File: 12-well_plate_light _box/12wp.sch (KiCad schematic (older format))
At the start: 7 parts

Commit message: added single well
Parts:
- U?: symbol SAM32:SAM32 -> 12wp-rescue:SAM32-SAM32
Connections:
- net labels added: OE
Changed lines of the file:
@@
 EESchema Schematic File Version 4
 LIBS:12wp-cache
-EELAYER 29 0
+EELAYER 30 0
 EELAYER END
 $Descr USLedger 17000 11000
@@
 	7700 7200 7900 7200
 $Comp
-L SAM32:SAM32 U?
+L 12wp-rescue:SAM32-SAM32 U?
 U 1 1 5E784C62
 P 7150 2200
@@
 Wire Wire Line
 	8350 6500 9400 6500
+Text Label 6350 2650 2    50   ~ 0
+OE
+Text Label 6900 7100 2    50   ~ 0
+OE
 $EndSCHEMATC

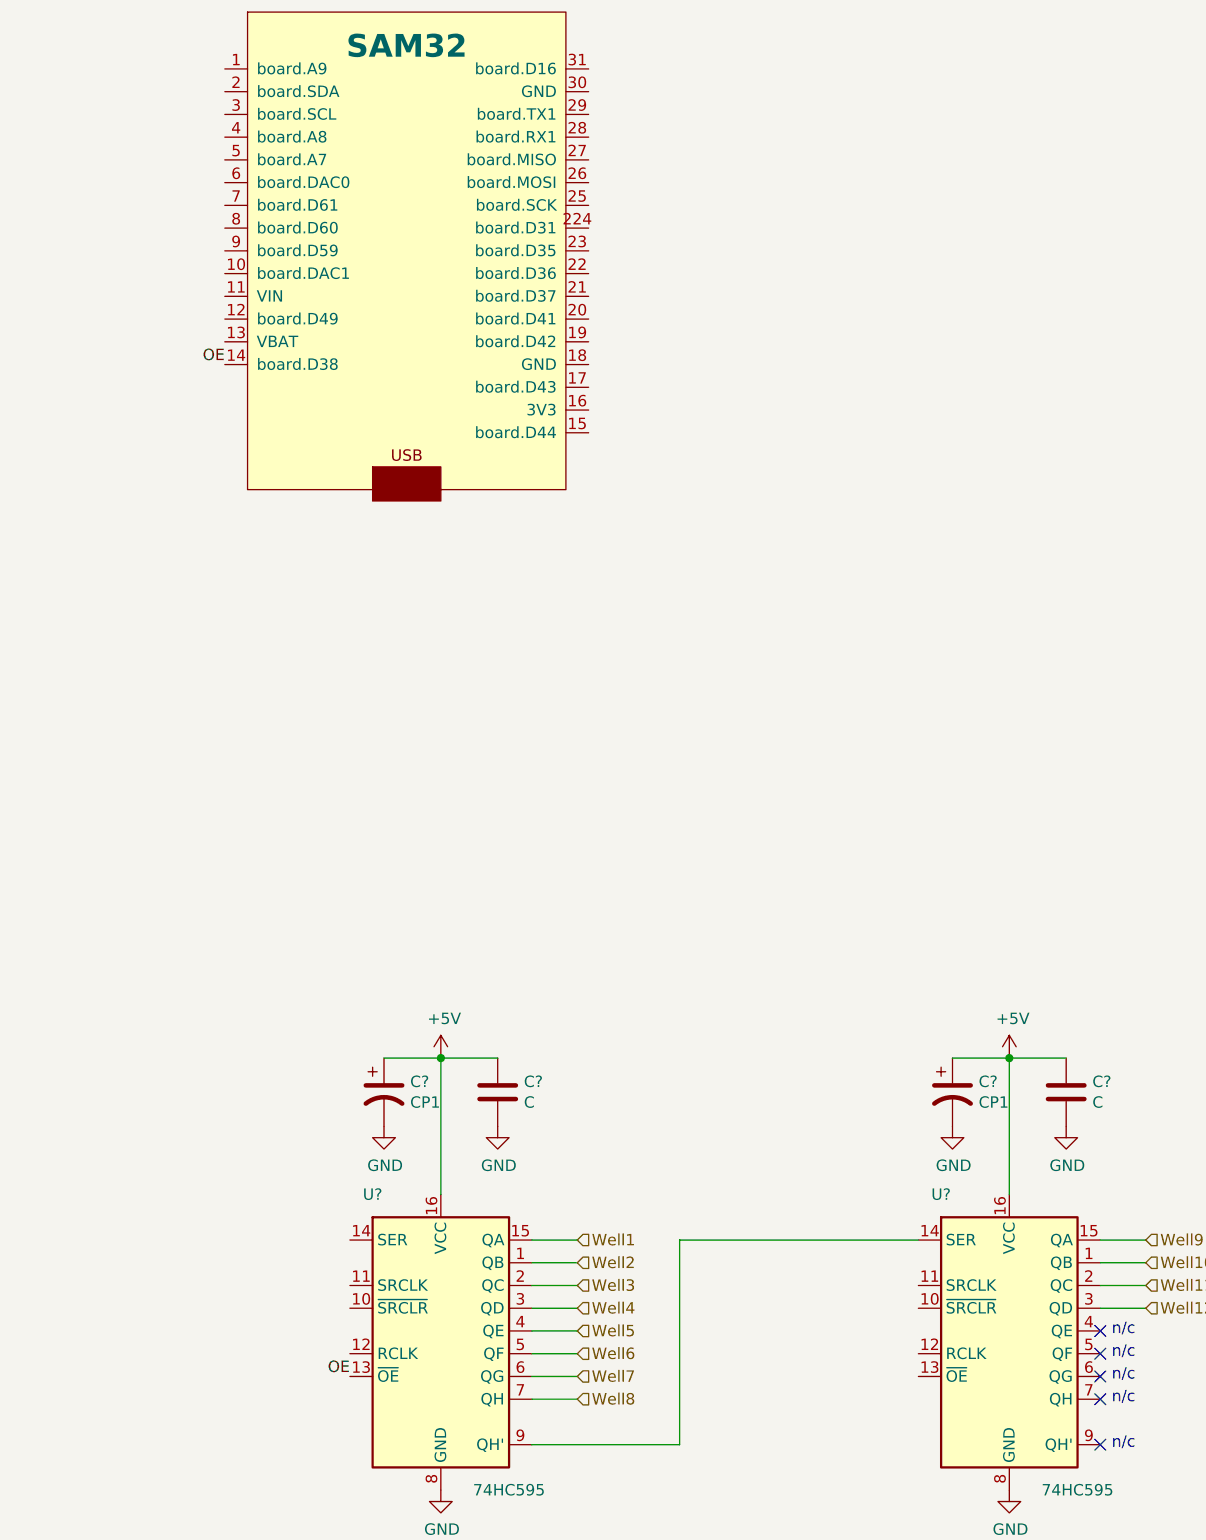
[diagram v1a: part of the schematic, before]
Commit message: added shift register controls
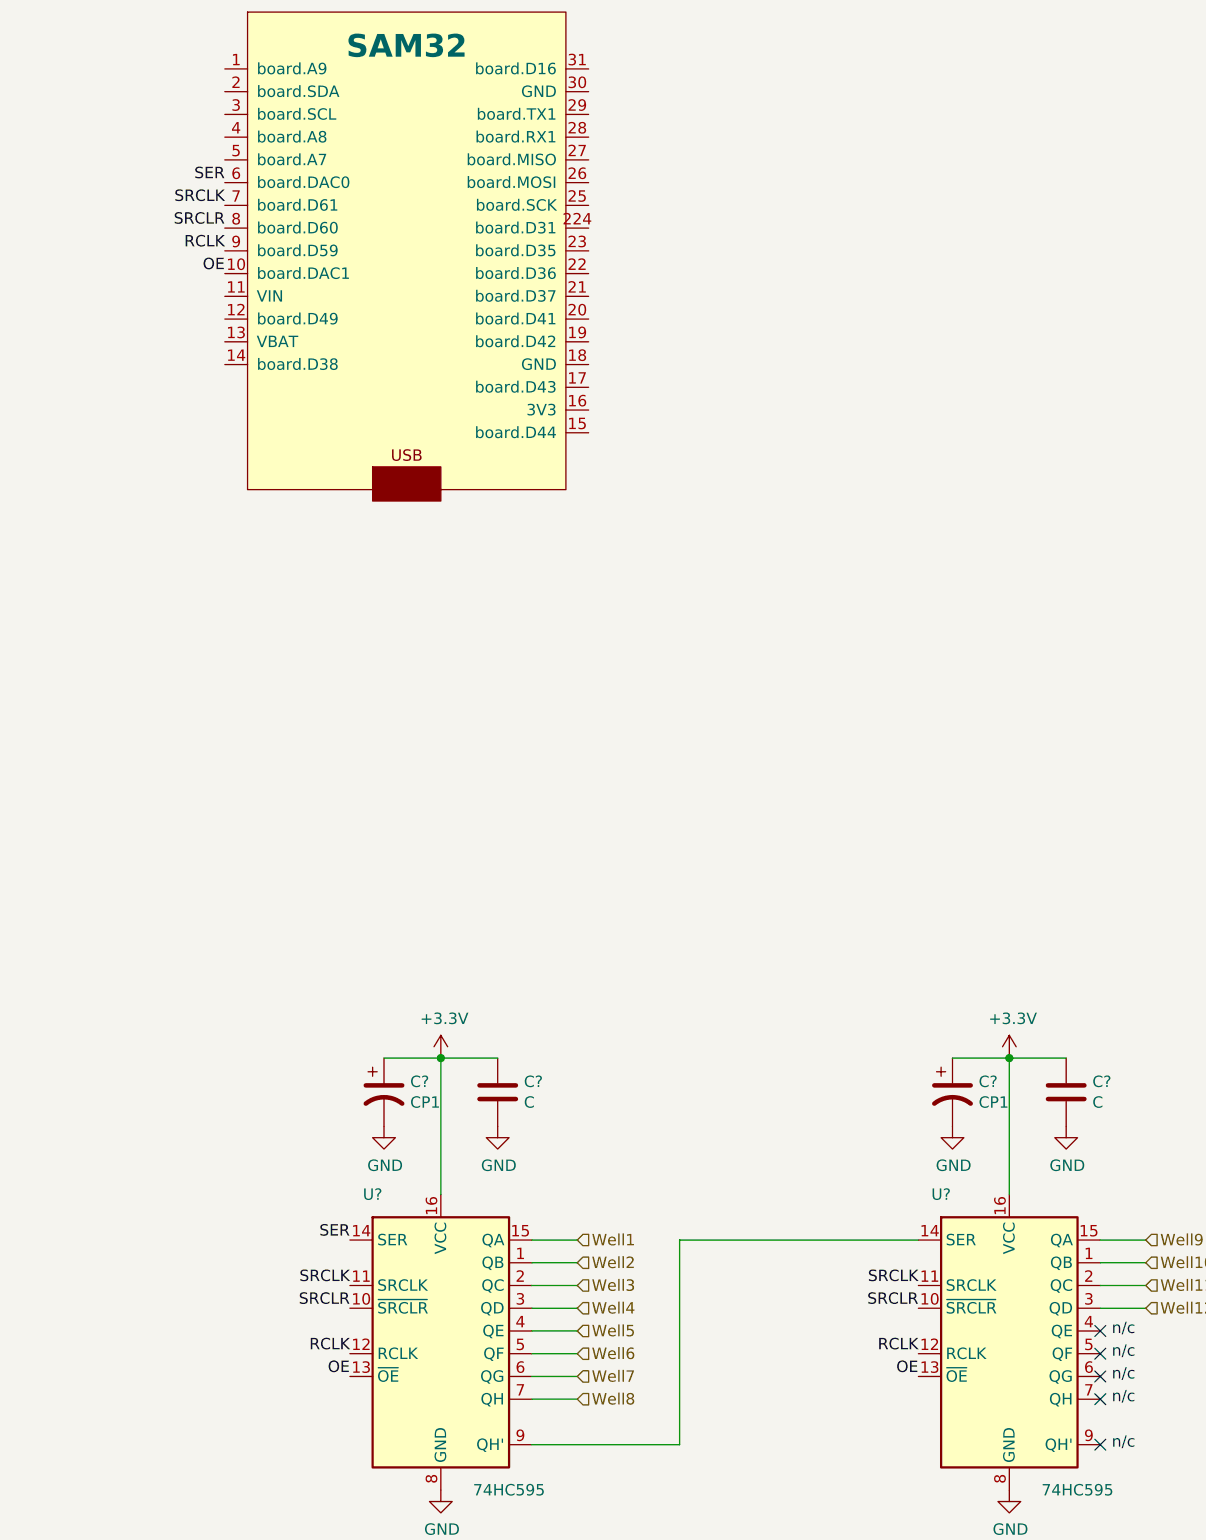
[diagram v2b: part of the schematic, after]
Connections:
- net OE: now also U?.10 (board.DAC1), U?.13 (~OE); no longer U?.14 (board.D38)
- net SRCLR: now reaches U?.10 (~SRCLR)
- net SRCLR: now also U?.10 (~SRCLR), U?.8 (board.D60)
- net SRCLK: now reaches U?.11 (SRCLK)
- net SRCLK: now also U?.11 (SRCLK), U?.7 (board.D61)
- net RCLK: now reaches U?.12 (RCLK)
- net RCLK: now also U?.12 (RCLK), U?.9 (board.D59)
- net SER: now reaches U?.14 (SER)
- net SER: now also U?.6 (board.DAC0)
- net +5V renamed +3V3
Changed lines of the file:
@@
 Power Section
-$Comp
-L power:+5V #PWR?
-U 1 1 5E74CEF4
-P 9800 5700
-AR Path="/5E423DD5/5E74CEF4" Ref="#PWR?"  Part="1"
-AR Path="/5E74CEF4" Ref="#PWR?"  Part="1"
-F 0 "#PWR?" H 9800 5550 50  0001 C CNN
-F 1 "+5V" H 9815 5873 50  0000 C CNN
-F 2 "" H 9800 5700 50  0001 C CNN
-F 3 "" H 9800 5700 50  0001 C CNN
-	1    9800 5700
-	1    0    0    -1
-$EndComp
 $Comp
 L Device:CP1 C?
@@
 $EndComp
 $Comp
-L power:+5V #PWR?
-U 1 1 5E750375
-P 7300 5700
-AR Path="/5E423DD5/5E750375" Ref="#PWR?"  Part="1"
-AR Path="/5E750375" Ref="#PWR?"  Part="1"
-F 0 "#PWR?" H 7300 5550 50  0001 C CNN
-F 1 "+5V" H 7315 5873 50  0000 C CNN
-F 2 "" H 7300 5700 50  0001 C CNN
-F 3 "" H 7300 5700 50  0001 C CNN
-	1    7300 5700
-	1    0    0    -1
-$EndComp
-$Comp
 L Device:CP1 C?
 U 1 1 5E75037B
@@
 Wire Wire Line
 	8350 6500 9400 6500
-Text Label 6350 2650 2    50   ~ 0
-OE
+$Comp
+L power:+3.3V #PWR?
+U 1 1 5E847CA7
+P 7300 5700
+F 0 "#PWR?" H 7300 5550 50  0001 C CNN
+F 1 "+3.3V" H 7315 5873 50  0000 C CNN
+F 2 "" H 7300 5700 50  0001 C CNN
+F 3 "" H 7300 5700 50  0001 C CNN
+	1    7300 5700
+	1    0    0    -1
+$EndComp
+$Comp
+L power:+3.3V #PWR?
+U 1 1 5E8482FC
+P 9800 5700
+F 0 "#PWR?" H 9800 5550 50  0001 C CNN
+F 1 "+3.3V" H 9815 5873 50  0000 C CNN
+F 2 "" H 9800 5700 50  0001 C CNN
+F 3 "" H 9800 5700 50  0001 C CNN
+	1    9800 5700
+	1    0    0    -1
+$EndComp
+Text Label 6350 1850 2    50   ~ 0
+SER
+Text Label 6350 1950 2    50   ~ 0
+SRCLK
+Text Label 6900 6700 2    50   ~ 0
+SRCLK
+Text Label 9400 6700 2    50   ~ 0
+SRCLK
+Text Label 6350 2050 2    50   ~ 0
+SRCLR
+Text Label 6900 6800 2    50   ~ 0
+SRCLR
+Text Label 9400 6800 2    50   ~ 0
+SRCLR
 Text Label 6900 7100 2    50   ~ 0
 OE
+Text Label 9400 7100 2    50   ~ 0
+OE
+Text Label 6350 2250 2    50   ~ 0
+OE
+Text Label 6900 6500 2    50   ~ 0
+SER
+Text Label 6900 7000 2    50   ~ 0
+RCLK
+Text Label 9400 7000 2    50   ~ 0
+RCLK
+Text Label 6350 2150 2    50   ~ 0
+RCLK
 $EndSCHEMATC
